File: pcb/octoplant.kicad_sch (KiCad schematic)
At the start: 27 parts, among them IC1 ATTINY824-SSFR, J1 Conn_01x03, SW1 SW_Push

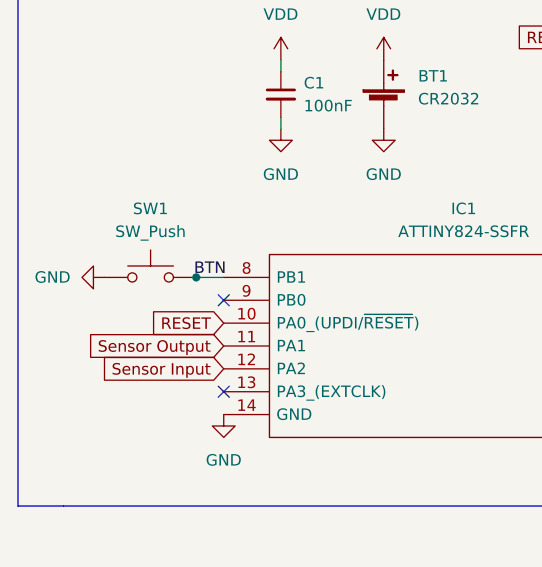
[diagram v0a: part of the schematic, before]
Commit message: Change button pin to a fully async one
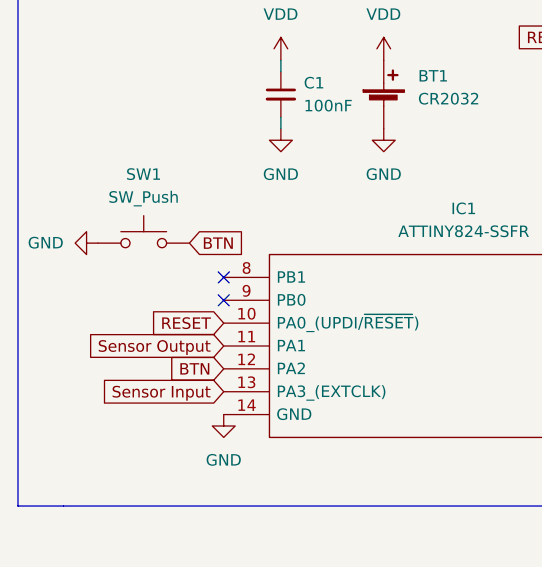
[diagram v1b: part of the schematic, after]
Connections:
- net BTN: now also IC1.12 (PA2); no longer IC1.8 (PB1)
- net Sensor Input: now also IC1.13 (PA3_(EXTCLK)); no longer IC1.12 (PA2)
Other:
- moved on the sheet: SW1
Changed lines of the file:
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@@
   (junction (at 81.28 153.67) (diameter 0) (color 0 0 0 0)
   )
-  (junction (at 57.912 82.55) (diameter 0) (color 0 0 0 0)
-  )
   (junction (at 229.87 86.36) (diameter 0) (color 0 0 0 0)
   )
@@
   (junction (at 262.89 59.69) (diameter 0) (color 0 0 0 0)
   )
-  (no_connect (at 60.96 95.25))
+  (no_connect (at 60.96 82.55))
   (no_connect (at 114.3 82.55))
   (no_connect (at 60.96 85.09))
@@
     (stroke (width 0) (type default) (color 0 0 0 0))
   )
-  (wire (pts (xy 57.912 82.55) (xy 60.96 82.55))
-    (stroke (width 0) (type default) (color 0 0 0 0))
-  )
   (polyline (pts (xy 153.67 40.64) (xy 153.67 105.41))
     (stroke (width 0) (type default) (color 0 0 0 0))
@@
   )
   (wire (pts (xy 171.45 59.69) (xy 173.99 59.69))
-    (stroke (width 0) (type default) (color 0 0 0 0))
-  )
-  (wire (pts (xy 57.658 82.55) (xy 57.912 82.55))
     (stroke (width 0) (type default) (color 0 0 0 0))
   )
@@
   (label "C_Soil_+" (at 81.28 161.29 180)
     (effects (font (size 1.27 1.27)) (justify right bottom))
-  )
-  (label "BTN" (at 57.658 82.55 0)
-    (effects (font (size 1.27 1.27)) (justify left bottom))
   )
   (global_label "LED Array 2" (shape input) (at 171.45 86.36 180) (fields_autoplaced)
@@
     )
   )
-  (global_label "Sensor Input" (shape input) (at 60.96 92.71 180) (fields_autoplaced)
-    (effects (font (size 1.27 1.27)) (justify right))
-    (property "Intersheet References" "${INTERSHEET_REFS}" (id 0) (at 46.3912 92.6306 0)
+  (global_label "Sensor Input" (shape input) (at 60.96 95.25 180) (fields_autoplaced)
+    (effects (font (size 1.27 1.27)) (justify right))
+    (property "Intersheet References" "${INTERSHEET_REFS}" (id 0) (at 46.3912 95.1706 0)
       (effects (font (size 1.27 1.27)) (justify right) hide)
     )
@@
     )
   )
+  (global_label "BTN" (shape input) (at 57.15 78.74 0) (fields_autoplaced)
+    (effects (font (size 1.27 1.27)) (justify left))
+    (property "Intersheet References" "${INTERSHEET_REFS}" (id 0) (at 63.1312 78.6606 0)
+      (effects (font (size 1.27 1.27)) (justify left) hide)
+    )
+  )
   (global_label "LED Array 3" (shape input) (at 171.45 100.33 180) (fields_autoplaced)
     (effects (font (size 1.27 1.27)) (justify right))
@@
     (effects (font (size 1.27 1.27)) (justify right))
     (property "Intersheet References" "${INTERSHEET_REFS}" (id 0) (at 52.8017 87.5506 0)
+      (effects (font (size 1.27 1.27)) (justify right) hide)
+    )
+  )
+  (global_label "BTN" (shape input) (at 60.96 92.71 180) (fields_autoplaced)
+    (effects (font (size 1.27 1.27)) (justify right))
+    (property "Intersheet References" "${INTERSHEET_REFS}" (id 0) (at 54.9788 92.6306 0)
       (effects (font (size 1.27 1.27)) (justify right) hide)
     )
@@
     (pin "2")
   )
-  (symbol (lib_id "power:GND") (at 47.752 82.55 270) (unit 1)
-    (in_bom yes) (on_board yes) (fields_autoplaced)
-    (property "Reference" "#PWR0107" (id 0) (at 41.402 82.55 0)
-      (effects (font (size 1.27 1.27)) hide)
-    )
-    (property "Value" "GND" (id 1) (at 43.942 82.5499 90)
+  (symbol (lib_id "power:GND") (at 46.99 78.74 270) (unit 1)
+    (in_bom yes) (on_board yes) (fields_autoplaced)
+    (property "Reference" "#PWR0107" (id 0) (at 40.64 78.74 0)
+      (effects (font (size 1.27 1.27)) hide)
+    )
+    (property "Value" "GND" (id 1) (at 43.18 78.7399 90)
       (effects (font (size 1.27 1.27)) (justify right))
     )
-    (property "Footprint" "" (id 2) (at 47.752 82.55 0)
-      (effects (font (size 1.27 1.27)) hide)
-    )
-    (property "Datasheet" "" (id 3) (at 47.752 82.55 0)
-      (effects (font (size 1.27 1.27)) hide)
-    )
-    (pin "1")
-  )
-  (symbol (lib_id "Switch:SW_Push") (at 52.832 82.55 0) (unit 1)
-    (in_bom yes) (on_board yes) (fields_autoplaced)
-    (property "Reference" "SW1" (id 0) (at 52.832 74.93 0))
-    (property "Value" "SW_Push" (id 1) (at 52.832 77.47 0))
-    (property "Footprint" "Button_Switch_SMD:SW_Push_1P1T_NO_CK_KSC6xxJ" (id 2) (at 52.832 77.47 0)
-      (effects (font (size 1.27 1.27)) hide)
-    )
-    (property "Datasheet" "~" (id 3) (at 52.832 77.47 0)
-      (effects (font (size 1.27 1.27)) hide)
-    )
+    (property "Footprint" "" (id 2) (at 46.99 78.74 0)
+      (effects (font (size 1.27 1.27)) hide)
+    )
+    (property "Datasheet" "" (id 3) (at 46.99 78.74 0)
+      (effects (font (size 1.27 1.27)) hide)
+    )
+    (pin "1")
+  )
+  (symbol (lib_id "Switch:SW_Push") (at 52.07 78.74 0) (unit 1)
+    (in_bom yes) (on_board yes) (fields_autoplaced)
+    (property "Reference" "SW1" (id 0) (at 52.07 71.12 0))
+    (property "Value" "SW_Push" (id 1) (at 52.07 73.66 0))
+    (property "Footprint" "Button_Switch_SMD:SW_Push_1P1T_NO_CK_KSC6xxJ" (id 2) (at 52.07 73.66 0)
+      (effects (font (size 1.27 1.27)) hide)
+    )
+    (property "Datasheet" "~" (id 3) (at 52.07 73.66 0)
+      (effects (font (size 1.27 1.27)) hide)
+    )

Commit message: resize capacitor pad
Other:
- title: (none) -> octo plant friend
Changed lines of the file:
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@@
 (kicad_sch (version 20211123) (generator eeschema)
   (paper "A4")
+  (title_block
+    (title "octo plant friend")
+    (date "2022-03-15")
+    (rev "1.0")
+  )
   (junction (at 229.87 59.69) (diameter 0) (color 0 0 0 0)
   )

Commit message: Tweak pcb
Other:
- note added: "Note in rev 1.0 this footprint is incorrect and is SC-80, this seems to be equivalent to SOD323"
- note added: "RED LED 150080RS75000 2V forward 30mA Ordered Yellow 224-9973 2V Forward"
- note removed: "RED LED 150080RS75000 2V forward 30mA"
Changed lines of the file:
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@@
     (stroke (width 0) (type default) (color 0 0 0 0))
   )
-  (text "RED LED 150080RS75000\n2V forward\n30mA" (at 165.1 49.53 0)
+  (text "Note in rev 1.0 this footprint is incorrect\nand is SC-80, this seems to be equivalent\n to SOD323\n"
+    (at 81.28 147.955 0)
     (effects (font (size 1.27 1.27)) (justify left bottom))
   )
+  (text "RED LED 150080RS75000\n2V forward\n30mA\n\nOrdered Yellow 224-9973\n2V Forward "
+    (at 165.1 49.53 0)
+    (effects (font (size 1.27 1.27)) (justify left bottom))
+  )
